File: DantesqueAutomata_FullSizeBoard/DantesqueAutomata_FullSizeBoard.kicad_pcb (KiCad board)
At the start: 2 copper layers, 90 x 110 mm, 112 parts, among them J1 DantesqueAutomata-Connector, J2 EurorackPower-Connector, U1 ESP32-DevKitC, U10 LM833, U11 LM833, U12 LM833, U2 GY-PCM5102, U3 GY-PCM5102, U4 LM833, U5 LM833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

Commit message: improved pcb design of full size board
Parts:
- removed the REF** at (136.0, 159.0)
- removed the REF** at (136.0, 57.0)
- removed the REF** at (54.0, 159.0)
- removed the REF** at (54.0, 57.0)
- added REF**: MountingHole_3.2mm_M3, MountingHole:MountingHole_3.2mm_M3, F.Cu at (111.0, 50.2)
- added REF**: MountingHole_3.2mm_M3, MountingHole:MountingHole_3.2mm_M3, F.Cu at (111.0, 153.0)
- added REF**: MountingHole_3.2mm_M3, MountingHole:MountingHole_3.2mm_M3, F.Cu at (193.8, 50.2)
- added REF**: MountingHole_3.2mm_M3, MountingHole:MountingHole_3.2mm_M3, F.Cu at (193.8, 153.0)
- J1: value DantesqueAutomata-Connector -> Dantesque_Automata_Connector; footprint Connector_PinHeader_2.54mm:PinHeader_2x17_P2.54mm_Vertical -> Connector_Eurorack:Dantesque_Automata_Connector
- J2: value EurorackPower-Connector -> Eurorack_16_Pin_Power; footprint Connector_PinHeader_2.54mm:PinHeader_2x08_P2.54mm_Vertical -> Connector_Eurorack:Eurorack_16_Pin_Power
- moved J1 84.0 mm to (152.4, 151.1), turned to -90 degrees
- moved J2 66.9 mm to (191.8, 101.6)
- moved R25 61.3 mm to (116.8, 48.3)
- moved R21 60.3 mm to (154.9, 48.3)
- moved R29 57.8 mm to (162.6, 68.6)
- moved U7 57.5 mm to (171.4, 63.5)
- moved C21 57.5 mm to (172.6, 70.5)
- moved C29 57.5 mm to (134.6, 70.5)
- moved C31 57.5 mm to (139.7, 78.7)
- moved C36 57.5 mm to (180.2, 64.7)
- moved C40 57.5 mm to (142.2, 64.7)
- moved C42 57.5 mm to (132.1, 78.7)
- moved R22 57.5 mm to (158.7, 62.2)
- moved R24 57.5 mm to (158.7, 64.8)
- moved R26 57.5 mm to (120.7, 62.2)
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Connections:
- net ADC_1 renamed ADC1
- net ADC_2 renamed ADC2
- net ADC_3 renamed ADC3
- net ADC_4 renamed ADC4
- net ADC_5 renamed ADC5
- net ADC_6 renamed ADC6
- net ADC_7 renamed ADC7
- net ADC_8 renamed ADC8
- net BCK_1 renamed BCK1
- net BCK_2 renamed BCK2
- net DAC_1 renamed DAC1
- net DAC_2 renamed DAC2
- net DIN_1 renamed DIN1
- net DIN_2 renamed DIN2
- net DOUT_1 renamed DOUT1
- net DOUT_2 renamed DOUT2
- net GPIO_1 renamed GPIO1
- net GPIO_2 renamed GPIO2
- net GPIO_3 renamed GPIO3
- net GPIO_4 renamed GPIO4
- net GPIO_5 renamed GPIO5
- net GPIO_6 renamed GPIO6
- net GPIO_7 renamed GPIO7
- net GPIO_8 renamed GPIO8
- net LD_A_IN_1 renamed LD_A_IN1
- net LD_A_IN_2 renamed LD_A_IN2
- net LD_A_IN_3 renamed LD_A_IN3
- net LD_A_IN_4 renamed LD_A_IN4
- net LD_A_IN_5 renamed LD_A_IN5
- net LD_A_IN_6 renamed LD_A_IN6
- net LD_A_IN_7 renamed LD_A_IN7
- net LD_A_IN_8 renamed LD_A_IN8
- net LD_A_OUT_1 renamed LD_A_OUT1
- net LD_A_OUT_2 renamed LD_A_OUT2
- net LIN_1 renamed LIN1
- net LIN_2 renamed LIN2
- net L_OUT_1 renamed LOUT1
- net L_OUT_2 renamed LOUT2
- net MCK_1 renamed MCK1
- net MCK_2 renamed MCK2
- net RIN_1 renamed RIN1
- net RIN_2 renamed RIN2
- net R_OUT_1 renamed ROUT1
- net R_OUT_2 renamed ROUT2
- net WS_1 renamed WS1
- net WS_2 renamed WS2
- J1 pad 1: +5V -> +12V
- J1 pad 2: +3.3V -> +12V
- J1 pad 3: +12V -> +3.3V
- J1 pad 4: +12V -> +5V
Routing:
- net GND: track 509.2 -> 74.6 mm, vias 9 -> 8
- net +3.3V: track 254.0 -> 357.3 mm, vias 14 -> 10
- net HD_A_IN1: track 167.8 -> 117.8 mm, vias 1 -> 5
- net +12V: track 239.3 -> 281.3 mm, vias 5 -> 11
- net GPIO8: track 62.7 -> 101.2 mm, vias 1 -> 3
- net HD_A_OUT3: track 78.5 -> 48.5 mm, vias 4 -> 2
- net HD_A_IN4: track 100.0 -> 129.2 mm, vias 2 -> 1
- net GPIO6: track 59.2 -> 87.0 mm, vias 1 -> 2
- net GPIO4: track 53.7 -> 79.7 mm, vias 1 -> 2
- net GPIO5: track 62.5 -> 85.2 mm, vias 2 -> 1
- net HD_A_IN3: track 131.1 -> 153.1 mm, vias 1 -> 3
- net HD_A_OUT1: track 49.7 -> 27.9 mm, vias 3 -> 1
- net GPIO1: track 33.7 -> 53.6 mm, vias 2 -> 1
- net -12V: track 380.4 -> 361.6 mm, vias 13 -> 9
- net Net-(C33-Pad2): track 118.4 -> 100.2 mm
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- added copper zone on B.Cu, net GND
- added copper zone on F.Cu, net GND

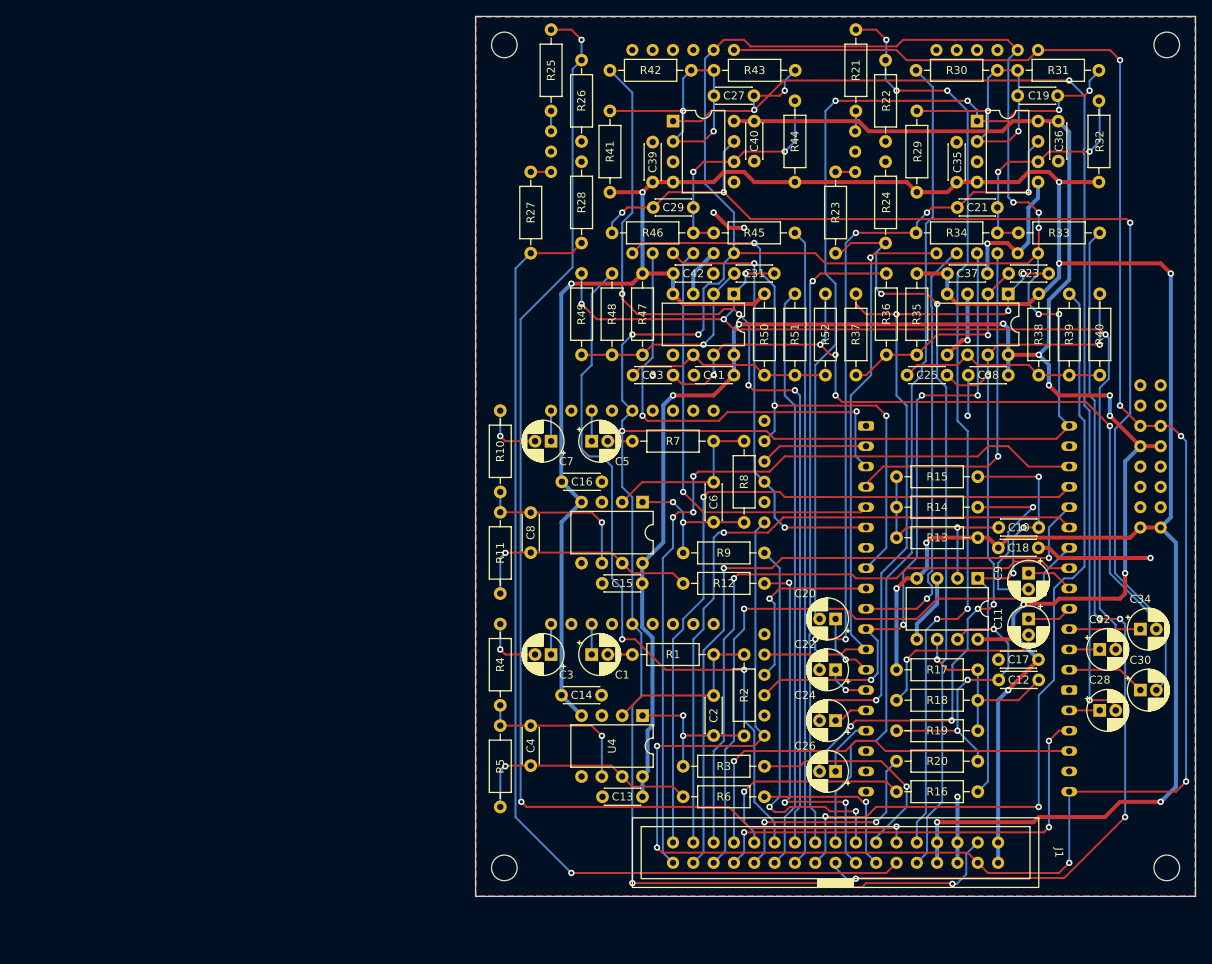
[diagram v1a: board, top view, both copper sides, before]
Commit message: fixed mounting holes
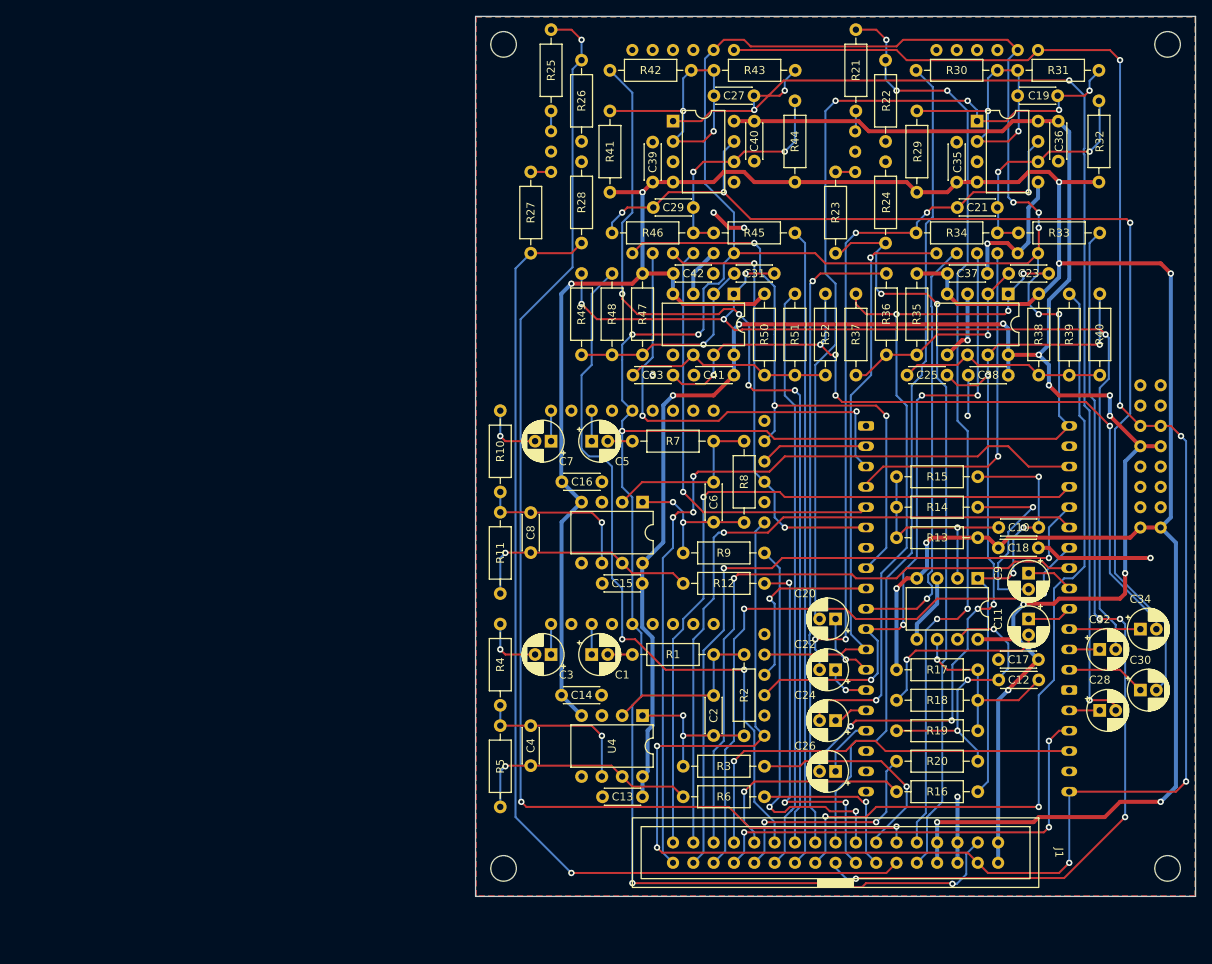
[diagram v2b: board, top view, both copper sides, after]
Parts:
- moved REF** 0.12 mm to (193.9, 50.1)
- moved REF** 0.12 mm to (193.9, 153.1)
- moved REF** 0.12 mm to (110.9, 50.1)
- moved REF** 0.12 mm to (110.9, 153.1)
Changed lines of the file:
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@@
   )
   (footprint "MountingHole:MountingHole_3.2mm_M3" (layer "F.Cu")
-    (at 110.998 50.165)
+    (at 110.9 50.1)
     (descr "Mounting Hole 3.2mm, no annular, M3")
     (tags "mounting hole 3.2mm no annular m3")
@@
   )
   (footprint "MountingHole:MountingHole_3.2mm_M3" (layer "F.Cu")
-    (at 110.998 153.035)
+    (at 110.9 153.1)
     (descr "Mounting Hole 3.2mm, no annular, M3")
     (tags "mounting hole 3.2mm no annular m3")
@@
   )
   (footprint "MountingHole:MountingHole_3.2mm_M3" (layer "F.Cu")
-    (at 193.802 50.165)
+    (at 193.9 50.1)
     (descr "Mounting Hole 3.2mm, no annular, M3")
     (tags "mounting hole 3.2mm no annular m3")
@@
   )
   (footprint "MountingHole:MountingHole_3.2mm_M3" (layer "F.Cu")
-    (at 193.802 153.035)
+    (at 193.9 153.1)
     (descr "Mounting Hole 3.2mm, no annular, M3")
     (tags "mounting hole 3.2mm no annular m3")

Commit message: increased drill hole size for board and footprints
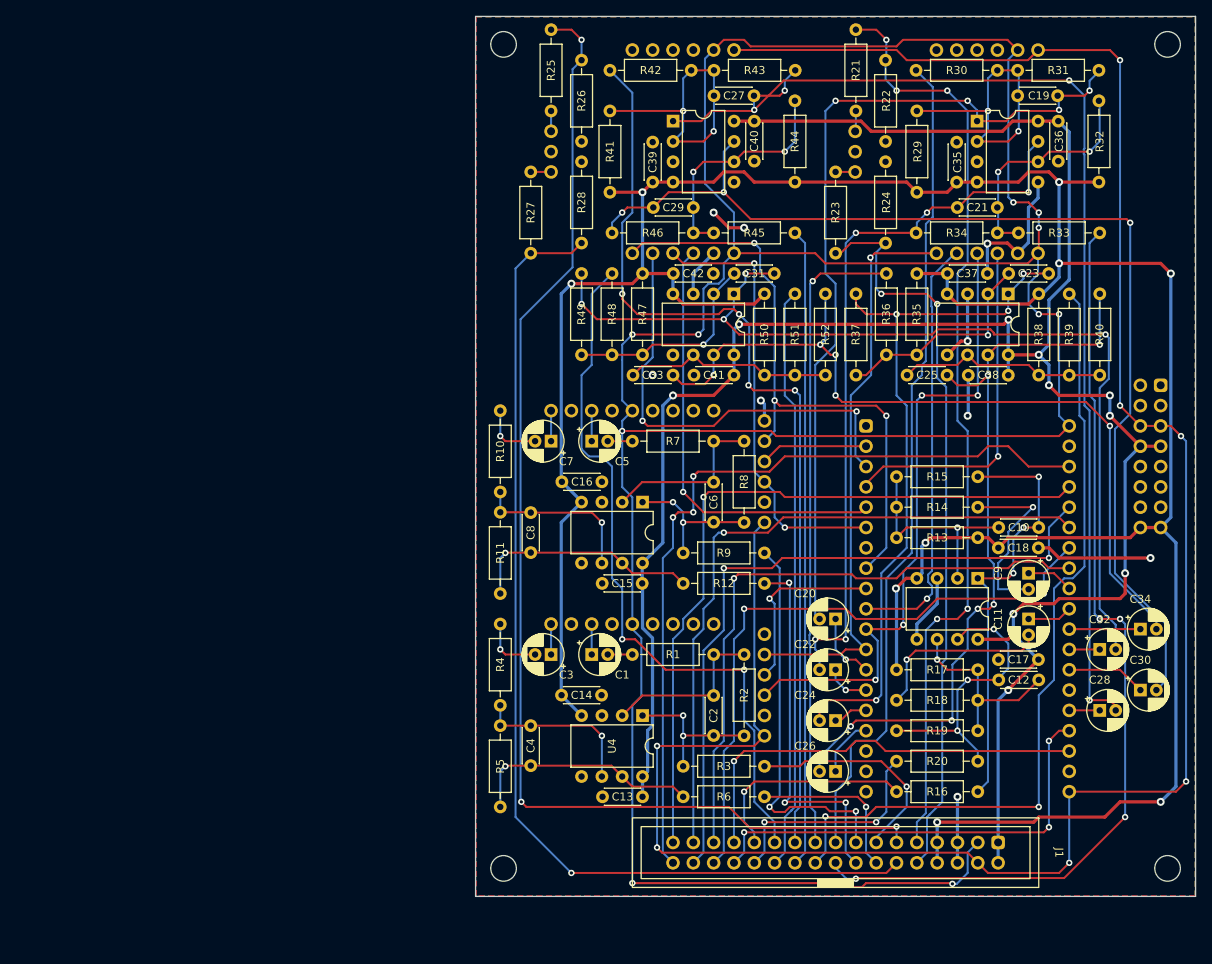
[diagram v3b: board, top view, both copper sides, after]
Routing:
- net GND: track 74.6 -> 77.4 mm, vias 8 -> 9
- net DIN2: track 55.9 -> 56.8 mm
- net +12V: track 281.3 -> 282.1 mm
- net Net-(C31-Pad2): track 122.2 -> 122.8 mm
